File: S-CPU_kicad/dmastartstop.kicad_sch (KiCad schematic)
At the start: 63 parts

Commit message: General update a
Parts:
- renumbered FMKL to OODF, FMKL to OOGP, FMKL to OOIO, FMKL to OOJS, FMKL to POHS, FMKL to POKF, FMKL to POLC, FMKL to POPO, FMKL to POQV, FMKL to POSI, FMKL to QOBA, FMKL to QOBN, FMKL to QOBT, FMKL to QOIS, SBRW to QOMK, FMKL to QONK, SBRW to QOSC, FMKL to QOXN, FMKL to ROLX, FMKL to RONJ, FMKL to ROOB, FMKL to ROSV, SBRW to SOMK, FMKL to SOMN, FMKL to SOXO, FMKL to SOZR, FMKL to UOTI, FMKL to UOTW, FMKL to VOJF
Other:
- note added: "If HDMA starts when GDMA is running, it will wait for the end of the current pattern or the end of transfer (whichever comes first) for HDMA to take over. GDMA will resume at the end of HDMA."
- note added: "This area seems to have a few mistakes that were corrected between revisions but left some unconnected tracks and stange routing: ROLX looks like it was originally clock by XIN/2 used by SOZR. O track is running very close to ROLX clk input is not conencted. CLK had to be brought from the bottwon right hand of the chip only to clock this DFF. QOYJ looks like an after thought.Layout almost suggest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"
- note removed: "If HDMA starts when GDMA is running, it will wait for the end of the current pattern HDMA to take over. GDMA will resume at the end of HDMA."
- moved on the sheet: SONJ

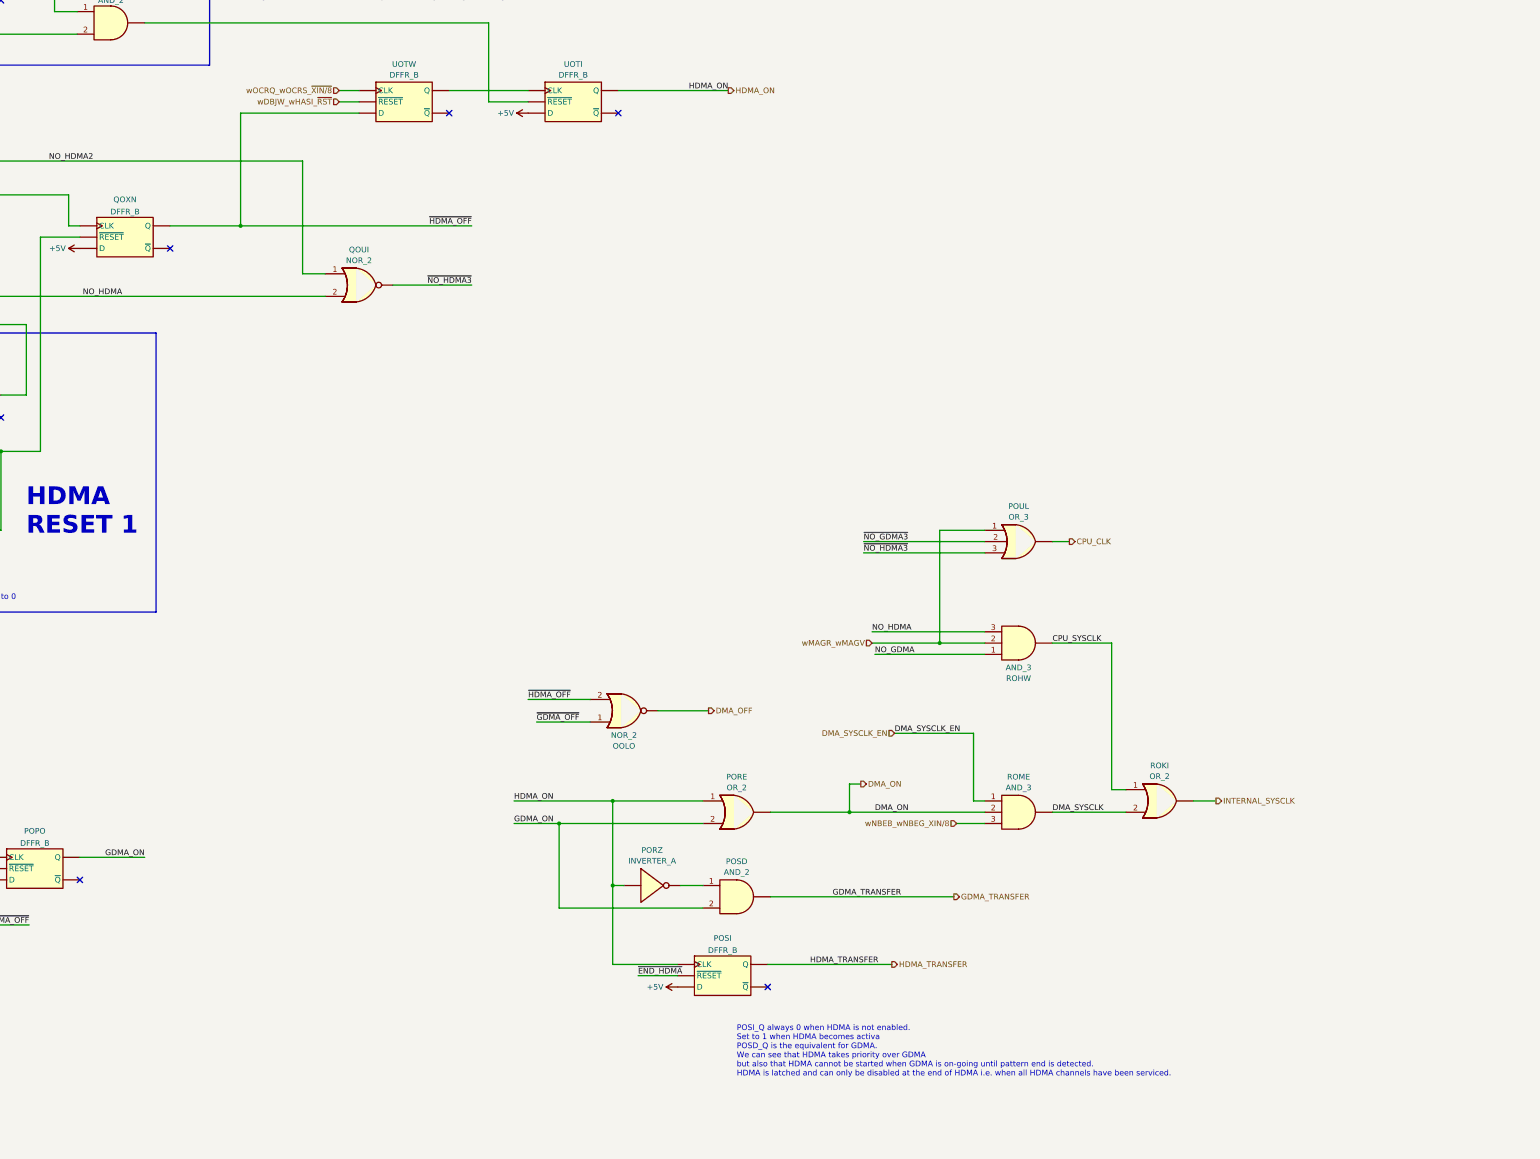
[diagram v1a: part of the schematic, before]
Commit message: More DMA updates - extra notes regarding behaviour
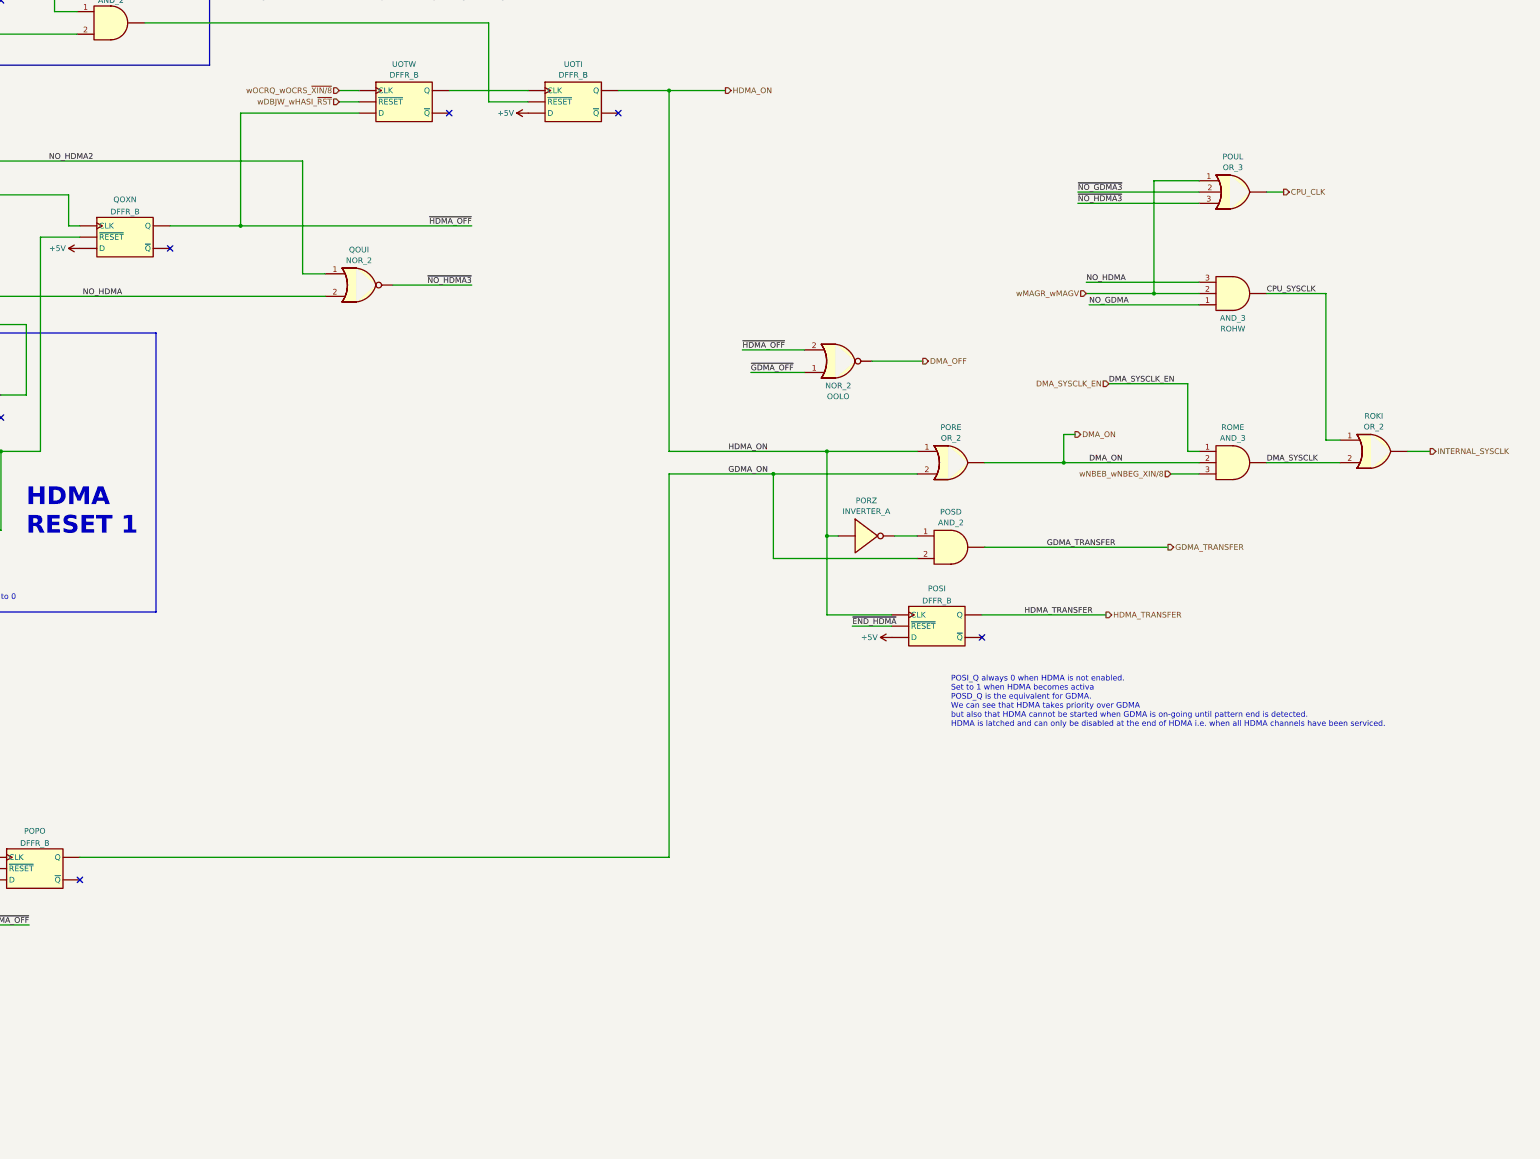
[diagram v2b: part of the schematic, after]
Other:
- moved on the sheet: OOLO, PORE, PORZ, POSD, POSI, POUL, ROHW, ROKI, ROME

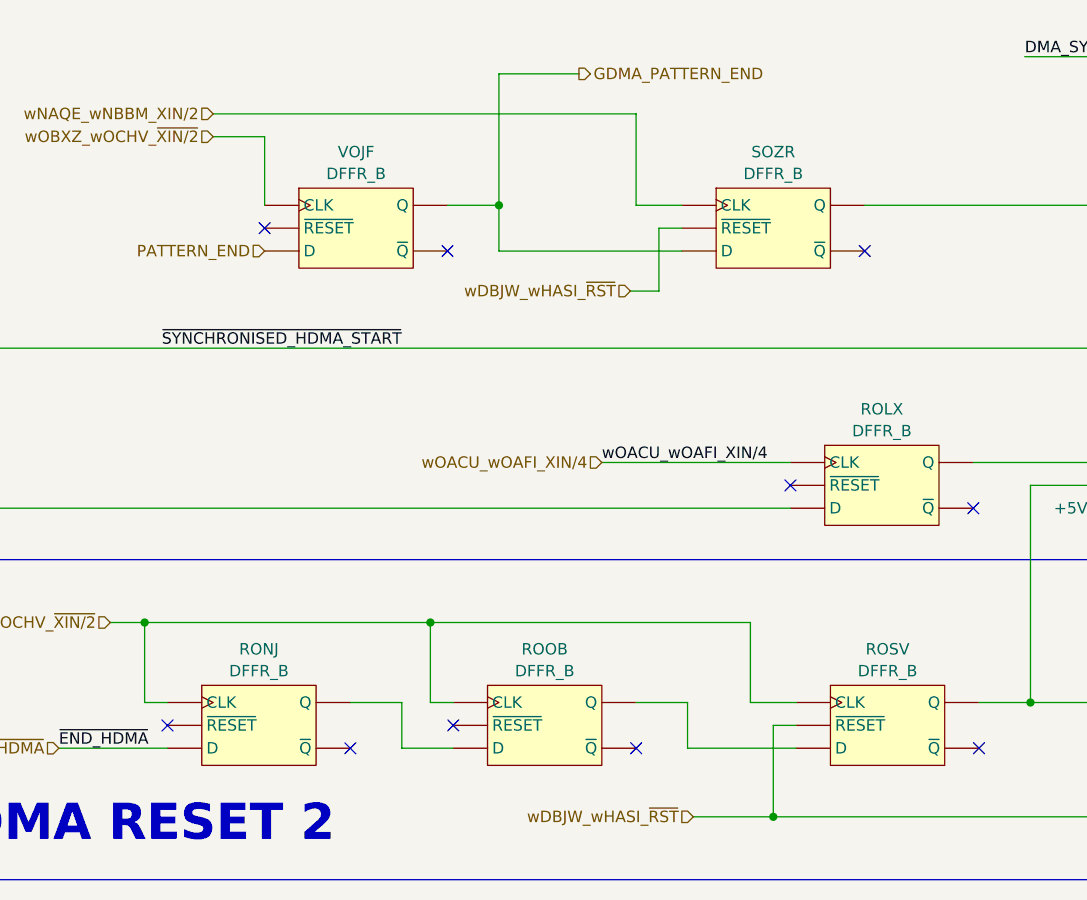
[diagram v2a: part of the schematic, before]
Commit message: Identified some DFFs as being DFFs with SET input rather than RESET input. It helps explaining a lot of beahiour in the MUL/DIV section and in the DMA section.
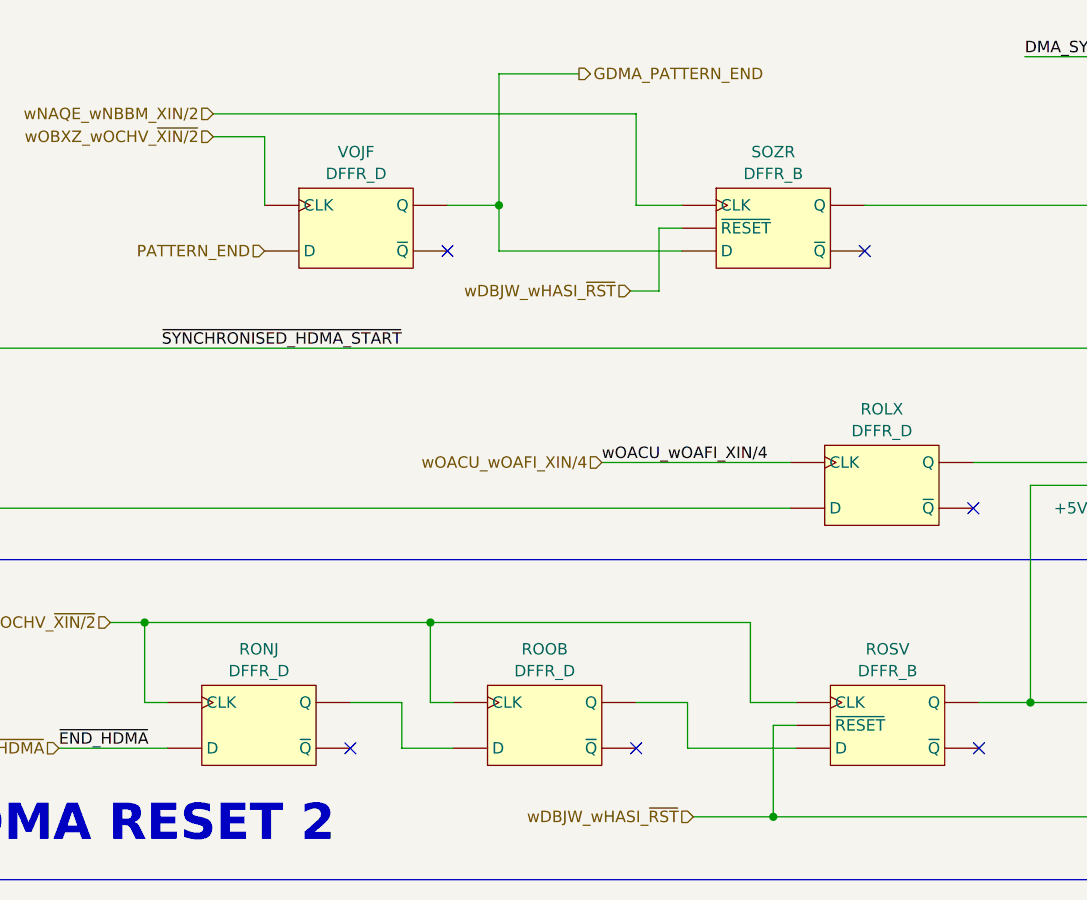
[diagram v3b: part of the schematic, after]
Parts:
- ROLX, RONJ, ROOB, VOJF: value DFFR_B -> DFFR_D; symbol Ricoh_Cells:DFFR_B -> Ricoh_Cells:DFFR_D
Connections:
- net GDMA_PATTERN_END: now also VOJF.8 (Q); no longer VOJF.7 (Q)
- net wOACU_wOAFI_XIN/4: now also ROLX.1 (CLK); no longer ROLX.3 (CLK), ROLX.4 (~{CLK})
- net wOBXZ_wOCHV_~{XIN/2}: now also RONJ.1 (CLK), ROOB.1 (CLK), VOJF.1 (CLK); no longer RONJ.3 (CLK), RONJ.4 (~{CLK}), ROOB.3 (CLK), ROOB.4 (~{CLK}), VOJF.3 (CLK), VOJF.4 (~{CLK})
- net at RONJ.7 (~{Q}): no longer ROOB.2 (D)
- net at ROOB.7 (~{Q}): no longer ROSV.2 (D)
- net at SOXO.3 (CLK), SOXO.4 (~{CLK}): now also ROLX.8 (Q); no longer ROLX.7 (Q)
- new net: RONJ.8 (Q), ROOB.2 (D)
- new net: ROOB.8 (Q), ROSV.2 (D)
- no-connect marks 41 -> 37
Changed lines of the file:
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@@
   (junction (at 302.895 480.06) (diameter 0) (color 0 0 0 0)
   )
-  (no_connect (at 375.285 208.28))
   (no_connect (at 384.175 453.39))
   (no_connect (at 452.755 269.875))
@@
   (no_connect (at 406.4 155.575))
   (no_connect (at 465.455 304.8))
-  (no_connect (at 407.035 208.28))
   (no_connect (at 131.445 193.04))
   (no_connect (at 414.655 316.23))
@@
   (no_connect (at 686.435 354.33))
   (no_connect (at 483.235 408.94))
-  (no_connect (at 386.08 153.035))
   (no_connect (at 83.185 183.515))
   (no_connect (at 464.82 184.15))
@@
   (no_connect (at 324.485 398.78))
   (no_connect (at 362.585 393.7))
-  (no_connect (at 444.5 181.61))
   (no_connect (at 363.855 282.575))
   (wire (pts (xy 471.17 205.74) (xy 477.52 205.74))
@@
     )
   )
-  (symbol (lib_id "Ricoh_Cells:DFFR_B") (at 385.445 208.28 0) (unit 1)
+  (symbol (lib_id "Ricoh_Cells:DFFR_D") (at 385.445 208.28 0) (unit 1)
     (in_bom yes) (on_board yes) (dnp no) (fields_autoplaced)
     (property "Reference" "RONJ" (at 385.445 199.8177 0)
       (effects (font (size 1.27 1.27)))
     )
-    (property "Value" "DFFR_B" (at 385.445 202.2419 0)
+    (property "Value" "DFFR_D" (at 385.445 202.2419 0)
       (effects (font (size 1.27 1.27)))
     )
@@
     (pin "1")
     (pin "2")
-    (pin "3")
-    (pin "4")
-    (pin "5")
-    (pin "6")
     (pin "7")
+    (pin "8")
     (instances
       (project "S-CPU"
@@
     )
   )
-  (symbol (lib_id "Ricoh_Cells:DFFR_B") (at 417.195 208.28 0) (unit 1)
+  (symbol (lib_id "Ricoh_Cells:DFFR_D") (at 417.195 208.28 0) (unit 1)
     (in_bom yes) (on_board yes) (dnp no) (fields_autoplaced)
     (property "Reference" "ROOB" (at 417.195 199.8177 0)
       (effects (font (size 1.27 1.27)))
     )
-    (property "Value" "DFFR_B" (at 417.195 202.2419 0)
+    (property "Value" "DFFR_D" (at 417.195 202.2419 0)
       (effects (font (size 1.27 1.27)))
     )
@@
     (pin "1")
     (pin "2")
-    (pin "3")
-    (pin "4")
-    (pin "5")
-    (pin "6")
     (pin "7")
+    (pin "8")
     (instances
       (project "S-CPU"
@@
     )
   )
-  (symbol (lib_id "Ricoh_Cells:DFFR_B") (at 454.66 181.61 0) (unit 1)
+  (symbol (lib_id "Ricoh_Cells:DFFR_D") (at 454.66 181.61 0) (unit 1)
     (in_bom yes) (on_board yes) (dnp no) (fields_autoplaced)
     (property "Reference" "ROLX" (at 454.66 173.1477 0)
       (effects (font (size 1.27 1.27)))
     )
-    (property "Value" "DFFR_B" (at 454.66 175.5719 0)
+    (property "Value" "DFFR_D" (at 454.66 175.5719 0)
       (effects (font (size 1.27 1.27)))
     )
@@
     (pin "1")
     (pin "2")
-    (pin "3")
-    (pin "4")
-    (pin "5")
-    (pin "6")
     (pin "7")
+    (pin "8")
     (instances
       (project "S-CPU"
@@
     )
   )
-  (symbol (lib_id "Ricoh_Cells:DFFR_B") (at 396.24 153.035 0) (unit 1)
+  (symbol (lib_id "Ricoh_Cells:DFFR_D") (at 396.24 153.035 0) (unit 1)
     (in_bom yes) (on_board yes) (dnp no) (fields_autoplaced)
     (property "Reference" "VOJF" (at 396.24 144.5727 0)
       (effects (font (size 1.27 1.27)))
     )
-    (property "Value" "DFFR_B" (at 396.24 146.9969 0)
+    (property "Value" "DFFR_D" (at 396.24 146.9969 0)
       (effects (font (size 1.27 1.27)))
     )
@@
     (pin "1")
     (pin "2")
-    (pin "3")
-    (pin "4")
-    (pin "5")
-    (pin "6")
     (pin "7")
+    (pin "8")
     (instances
       (project "S-CPU"

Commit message: Fix ERC errors in schematics.
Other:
- company: (none) -> Author: Regis Galland
- title: (none) -> Reverse Engineered SNES S-CPU Schematics 
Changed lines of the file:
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@@
 (kicad_sch (version 20230121) (generator eeschema)
   (paper "A1")
+  (title_block
+    (title "Reverse Engineered SNES S-CPU Schematics ")
+    (date "2023-10-21")
+    (rev "0.1")
+    (company "Author: Regis Galland")
+  )
   (junction (at 518.795 145.415) (diameter 0) (color 0 0 0 0)
   )

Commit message: Big rework on the hierachical sheet to make thigs a bit clearer. PDF exported for Rev 0.1.
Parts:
- renumbered OBEE to QOYJ, OBEE to SOZO
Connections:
- net DMA_SYSCLK: now also NBIV.1 (CLK), NBIZ.1 (CLK), OBHN.1 (CLK), OBIW.1 (CLK), OOGP.1 (CLK), OOIO.1 (CLK), POGD.1, POLC.1 (CLK), POUL.1, QOBT.1 (CLK), QONK.1 (CLK), QOSC.1 (CLK), ROHW.2; no longer ROKI.2, ROME.4
- net GDMA_ON: now also POPO.9 (Q); no longer POPO.7 (Q)
- net HDMA_ON: now also POSI.1 (CLK), UOTI.9 (Q); no longer POSI.3 (CLK), POSI.4 (~{CLK}), UOTI.7 (Q)
- net HDMA_TRANSFER: now also POSI.9 (Q); no longer POSI.7 (Q)
- net NO_GDMA: now also OODF.8 (~{Q}); no longer OODF.6 (~{Q})
- net NO_GDMA2: now also OOIO.9 (Q); no longer OOIO.7 (Q)
- net NO_HDMA: now also QOMK.9 (~{Q}); no longer QOMK.4 (~{Q})
- net NO_HDMA2: now also QOSC.11 (Q); no longer QOSC.5 (Q)
- net ~{END_HDMA}: now also POSI.6 (~{RESET}), SOMK.7 (~{RESET}); no longer POSI.1 (~{RESET}), POSI.5 (~{RESET}), SOMK.6 (~{RESET})
- net ~{GDMA_OFF}: now also OOJS.9 (Q); no longer OOJS.7 (Q)
- net ~{HDMA_OFF}: now also QOXN.9 (Q); no longer QOXN.7 (Q)
- net ~{SYNCHRONISED_HDMA_START}: now also QOMK.4 (~{SET}), QOSC.7 (~{RESET}), SOMK.4 (~{SET}); no longer QOMK.1 (~{SET}), QOMK.3 (~{SET}), QOSC.6 (~{RESET}), SOMK.1 (~{SET}), SOMK.3 (~{SET})
- net at SOXY.3, SOZA.1: now also SOXO.9 (Q); no longer SOXO.7 (Q)
- net at QOHV.1: now also QOBT.8 (~{Q}); no longer QOBT.6 (~{Q})
- net at QOBT.2 (D), QOHV.2: now also QOBN.9 (Q); no longer QOBN.7 (Q)
- net at POOO.1: now also POLC.8 (~{Q}); no longer POLC.6 (~{Q})
- net at POLC.2 (D), POOO.2: now also POKF.9 (Q); no longer POKF.7 (Q)
- net at OOGP.2 (D), POOO.3: now also OOJS.6 (~{RESET}); no longer OOJS.1 (~{RESET}), OOJS.5 (~{RESET})
- net at NBIE.1, NBIV.2 (D): now also NBIZ.9 (Q); no longer NBIZ.7 (Q)
- net at NBIV.6 (~{RESET}): no longer NBIE.2
- net at QOBA.2 (D), QOIS.2 (D): now also SOMK.11 (Q); no longer SOMK.5 (Q)
- net ~{MRST}: now reaches QOIS.6 (~{RESET})
- net ~{MRST}: now also OOBX.6 (~{RESET}), OOGP.6 (~{RESET}), OOIO.6 (~{RESET}), POHS.6 (~{RESET}), POKF.6 (~{RESET}), POLC.6 (~{RESET}), POPB.2, POQV.6 (~{RESET}), QOBA.6 (~{RESET}), QOBN.6 (~{RESET}), QOBT.6 (~{RESET}), QONK.6 (~{RESET}), QOSC.4 (~{SET}), QOYJ.2, ROSV.6 (~{RESET}), SOMN.6 (~{RESET}), SOZR.6 (~{RESET}), UOTW.6 (~{RESET})
- net at QOMK.7 (~{RESET}): now also QONK.9 (Q); no longer QOIS.7 (Q)
- net at NBIZ.2 (D): now also OAOU.9 (Q); no longer OAOU.6 (Q)
- net at OBEQ.1, OBHN.2 (D): now also OBIW.9 (Q); no longer OBIW.7 (Q)
- net at OBHN.6 (~{RESET}): no longer OBEQ.2
- net at SOXO.6 (~{RESET}): now also QOYJ.1, ROSV.9 (Q)
- net at OBEE.3, QONK.2 (D): now also QOXN.6 (~{RESET}); no longer QOXN.1 (~{RESET}), QOXN.5 (~{RESET})
- net at POKF.2 (D), POPB.1: now also POHS.9 (Q); no longer POHS.7 (Q)
- net at QOBN.2 (D): now also QOBA.9 (Q); no longer QOBA.7 (Q)
- net at UOTI.6 (~{RESET}): now also QOYJ.3
- net at POPO.6 (~{RESET}): now also POPB.3
- net DMA_XIN/8: now reaches OAOU.1 (CLK)
- net DMA_XIN/8: now also ROME.3; no longer OAOU.5 (~{RESET})
- net at SOZA.3: now also SOZR.9 (Q); no longer SOZR.7 (Q)
- removed net wDBJW_wHASI_~{RST}: OOBX.1 (~{RESET}), OOBX.5 (~{RESET}), OOGP.1 (~{RESET}), OOGP.5 (~{RESET}), OOIO.1 (~{RESET}), OOIO.5 (~{RESET}), POHS.1 (~{RESET}), POHS.5 (~{RESET}), POKF.1 (~{RESET}), POKF.5 (~{RESET}), POLC.1 (~{RESET}), POLC.5 (~{RESET}), POPB.2, POQV.1 (~{RESET}), POQV.5 (~{RESET}), QOBA.1 (~{RESET}), QOBA.5 (~{RESET}), QOBN.1 (~{RESET}), QOBN.5 (~{RESET}), QOBT.1 (~{RESET}), QOBT.5 (~{RESET}), QOIS.1 (~{RESET}), QOIS.5 (~{RESET}), QONK.1 (~{RESET}), QONK.5 (~{RESET}), QOSC.1 (~{SET}), QOSC.3 (~{SET}), QOYJ.2, ROSV.1 (~{RESET}), ROSV.5 (~{RESET}), SOMN.1 (~{RESET}), SOMN.5 (~{RESET}), SOZR.1 (~{RESET}), SOZR.5 (~{RESET}), UOTW.1 (~{RESET}), UOTW.5 (~{RESET})
- removed net wMAGR_wMAGV: NBIV.3 (CLK), NBIV.4 (~{CLK}), NBIZ.3 (CLK), NBIZ.4 (~{CLK}), OBHN.3 (CLK), OBHN.4 (~{CLK}), OBIW.3 (CLK), OBIW.4 (~{CLK}), OOGP.3 (CLK), OOGP.4 (~{CLK}), OOIO.3 (CLK), OOIO.4 (~{CLK}), POGD.1, POLC.3 (CLK), POLC.4 (~{CLK}), POUL.1, QOBT.3 (CLK), QOBT.4 (~{CLK}), QONK.3 (CLK), QONK.4 (~{CLK}), QOSC.7 (CLK), ROHW.2
- removed net wNAGK_wNAJD: POKF.3 (CLK), POKF.4 (~{CLK}), QOBN.3 (CLK), QOBN.4 (~{CLK})
- removed net wNAQE_wNBBM_XIN/2: SOZR.3 (CLK), SOZR.4 (~{CLK})
- removed net wNBEB_wNBEG_XIN/8: OAOU.3 (CLK), OAOU.4 (~{CLK}), ROME.3
- net wOACU_wOAFI_XIN/4 renamed DMA_XIN/4
- net wOBXZ_wOCHV_~{XIN/2} renamed DMA_~{XIN/2}
- net DMA_~{XIN/2}: now also ROSV.1 (CLK); no longer ROSV.3 (CLK), ROSV.4 (~{CLK})
- removed net wOCRQ_wOCRS_~{XIN/8}: POHS.3 (CLK), POHS.4 (~{CLK}), POQV.3 (CLK), POQV.4 (~{CLK}), QOBA.3 (CLK), QOBA.4 (~{CLK}), UOTW.3 (CLK), UOTW.4 (~{CLK})
- new net: OOIO.8 (~{Q}), OOJS.1 (CLK)
- new net: NBIE.2, NBIV.8 (~{Q})
- new net: OOBX.1 (CLK), POGD.2, QOIS.1 (CLK), SOMN.1 (CLK)
- new net: QOIS.9 (Q), QOMK.1 (CLK)
- new net: OOBX.9 (Q), OODF.1 (CLK)
- new net: POPO.1 (CLK), POQV.9 (Q)
- new net: SOMK.1 (CLK), SOMN.9 (Q)
- new net: QOSC.9 (~{Q}), QOXN.1 (CLK)
- new net: OBEQ.2, OBHN.8 (~{Q})
- new net: ROLX.8 (Q), SOXO.1 (CLK)
- new net: OODF.6 (~{RESET}), OOGP.9 (Q)
- new net: ROKI.2, ROME.4
- new net: UOTI.1 (CLK), UOTW.9 (Q)
- new net DMA_XIN/2: SOZR.1 (CLK)
- new net DMA_~{XIN/8}: POHS.1 (CLK), POQV.1 (CLK), QOBA.1 (CLK), UOTW.1 (CLK)
- new net ~{DMA_SYSCLK}: POKF.1 (CLK), QOBN.1 (CLK)
